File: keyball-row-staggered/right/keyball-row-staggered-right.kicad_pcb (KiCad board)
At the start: 2 copper layers, 178.2 x 113.8 mm, 91 parts, among them J11 trackball, J12 MJ-4PP-9, SW1 SW_PUSH, SW10 SW_PUSH, SW11 SW_PUSH, SW12 SW_PUSH, SW13 SW_PUSH, SW14 SW_PUSH, SW15 SW_PUSH, SW16 SW_PUSH, SW17 SW_PUSH, SW18 SW_PUSH, SW19 SW_PUSH, SW2 SW_PUSH, SW20 SW_PUSH, SW21 SW_PUSH, SW22 SW_PUSH, SW23 SW_PUSH, SW24 SW_PUSH, SW25 SW_PUSH, SW26 SW_PUSH, SW27 SW_PUSH, SW28 SW_PUSH, SW29 SW_PUSH, SW3 SW_PUSH, SW30 SW_PUSH, SW31 SW_PUSH, SW32 SW_PUSH, SW33 SW_PUSH, SW34 SW_PUSH, SW4 SW_PUSH, SW5 SW_PUSH, SW6 SW_PUSH, SW7 SW_PUSH, SW8 SW_PUSH, SW9 SW_PUSH, U1 ProMicro

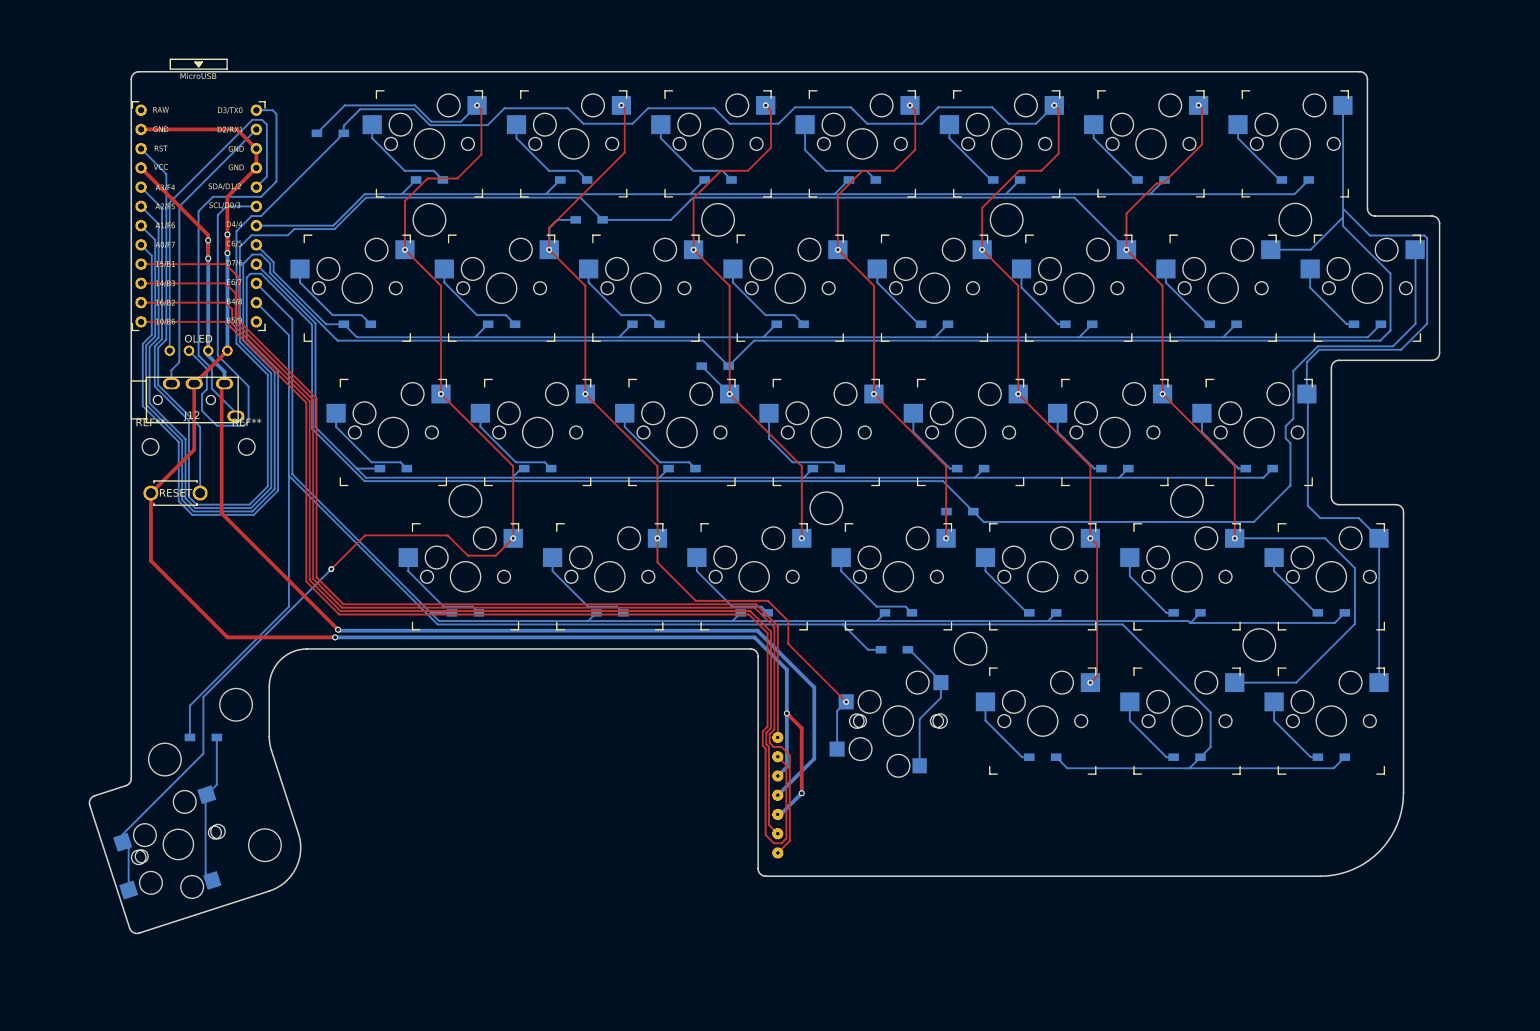
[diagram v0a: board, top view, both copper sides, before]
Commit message: add order-number placeholder
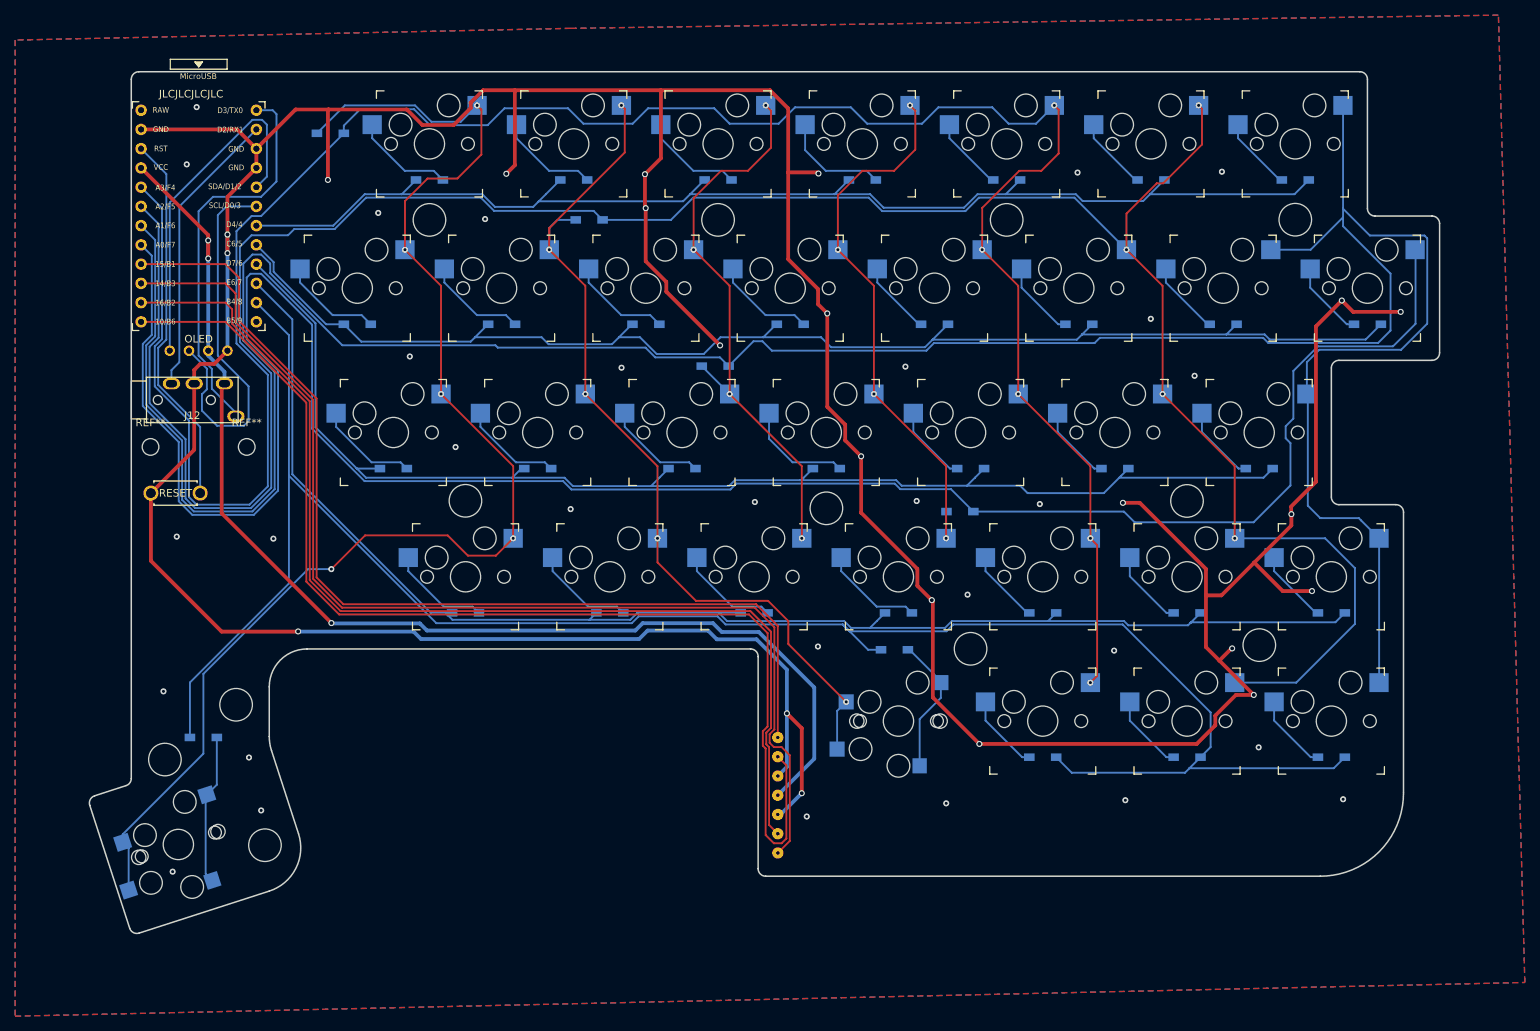
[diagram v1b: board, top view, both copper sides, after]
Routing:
- net GND: track 199.1 -> 576.4 mm, vias 5 -> 52
- net ROW2: track 166.4 -> 172.5 mm
- net ROW0: track 157.5 -> 162.6 mm
- net ROW1: track 170.0 -> 173.8 mm
- net ROW4: track 253.5 -> 255.5 mm
- net ROW3: track 185.8 -> 187.6 mm
- net Net-(D35-A): track 176.3 -> 178.1 mm
- net COL2: track 380.6 -> 382.2 mm
- net COL1: track 325.7 -> 327.2 mm
- net VCC: track 156.7 -> 157.5 mm
- net COL3: track 287.9 -> 288.5 mm
- added copper zone on B.Cu, net GND
- added copper zone on F.Cu, net GND
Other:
- board text added: "JLCJLCJLCJLC"

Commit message: 右手配置修正
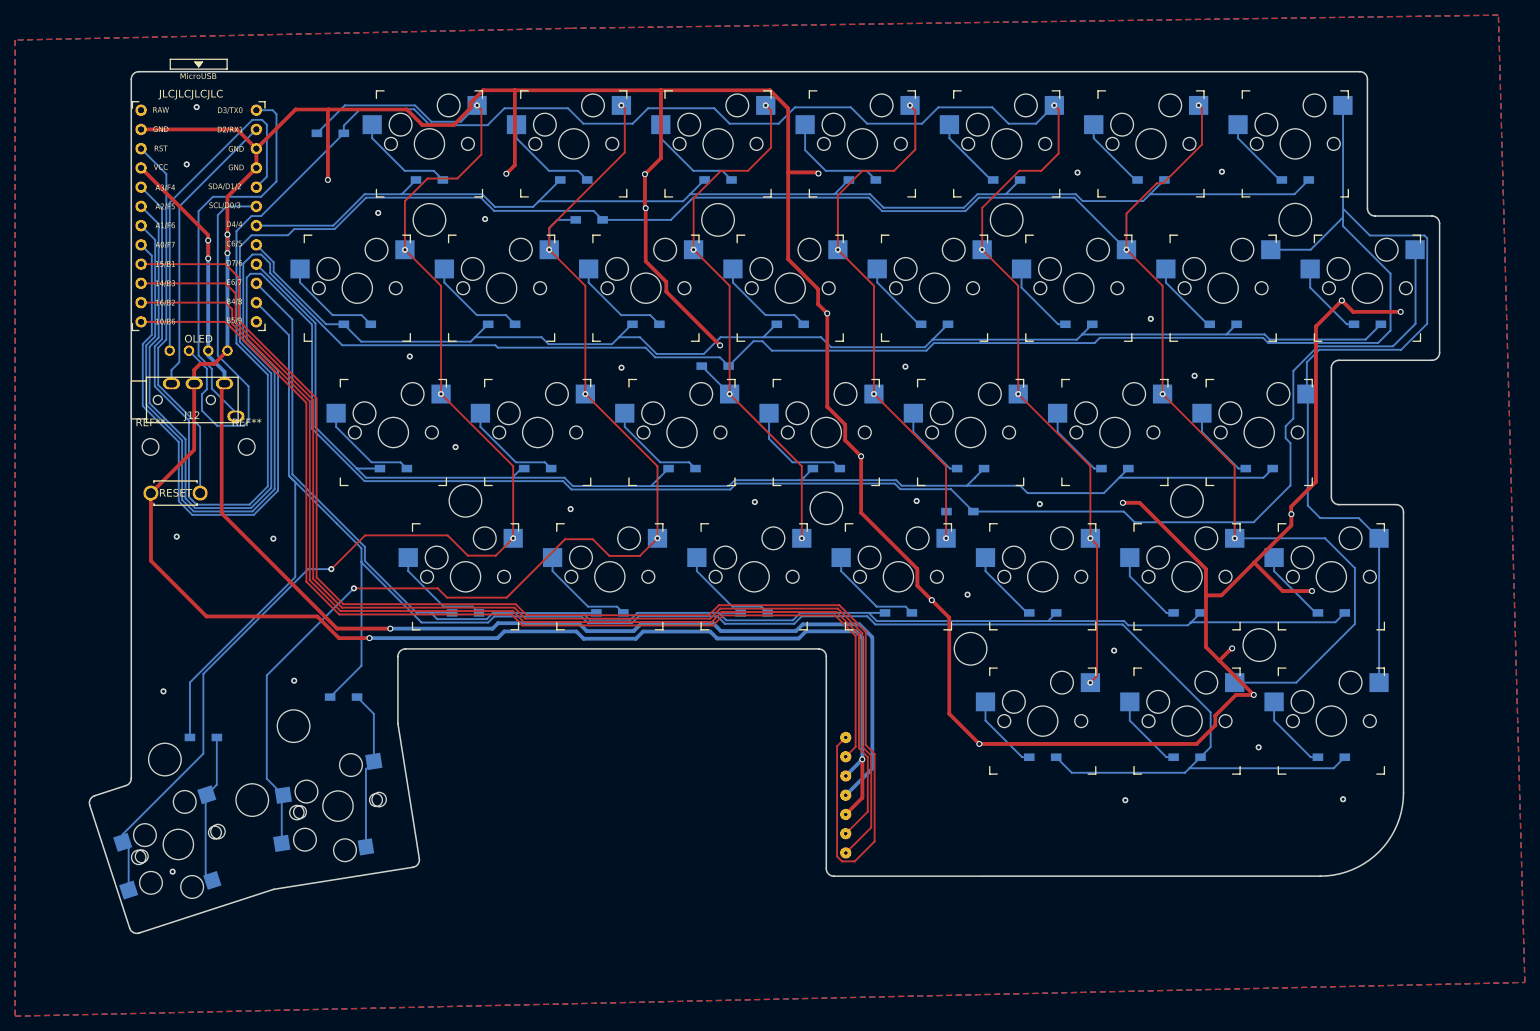
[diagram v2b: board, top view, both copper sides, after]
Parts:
- moved SW31 74.8 mm to (73.6, 135.0), turned to 9 degrees
- moved D31 73.0 mm to (74.4, 120.7)
- moved J11 8.97 mm to (140.9, 133.6)
- moved Ref** 8.10 mm to (67.8, 124.5)
- moved Ref** 6.19 mm to (62.3, 134.2)
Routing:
- net SCLK: track 135.8 -> 184.7 mm
- net Net-(D36-A): track 118.4 -> 159.2 mm
- net ROW4: track 255.5 -> 271.2 mm
- net MOSI: track 143.7 -> 157.0 mm
- net NCS: track 155.3 -> 142.9 mm
- net VCC: track 157.5 -> 169.9 mm
- net MISO: track 150.9 -> 162.4 mm
- net GND: track 576.4 -> 583.1 mm, vias 52 -> 47
- net ROW3: track 187.6 -> 191.4 mm
- net Net-(D31-K): track 18.4 -> 21.1 mm
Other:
- outline, holes or cut-outs redrawn
